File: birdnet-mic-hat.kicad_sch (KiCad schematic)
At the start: 28 parts, among them J1 PJ-327A0-SMT, J3 DF40HC(3.5)-30DS-0.4V(51), U1 TLV320ADC5140, U2 TPS7A2033PDBVR, U3 TLV3691IDCKR

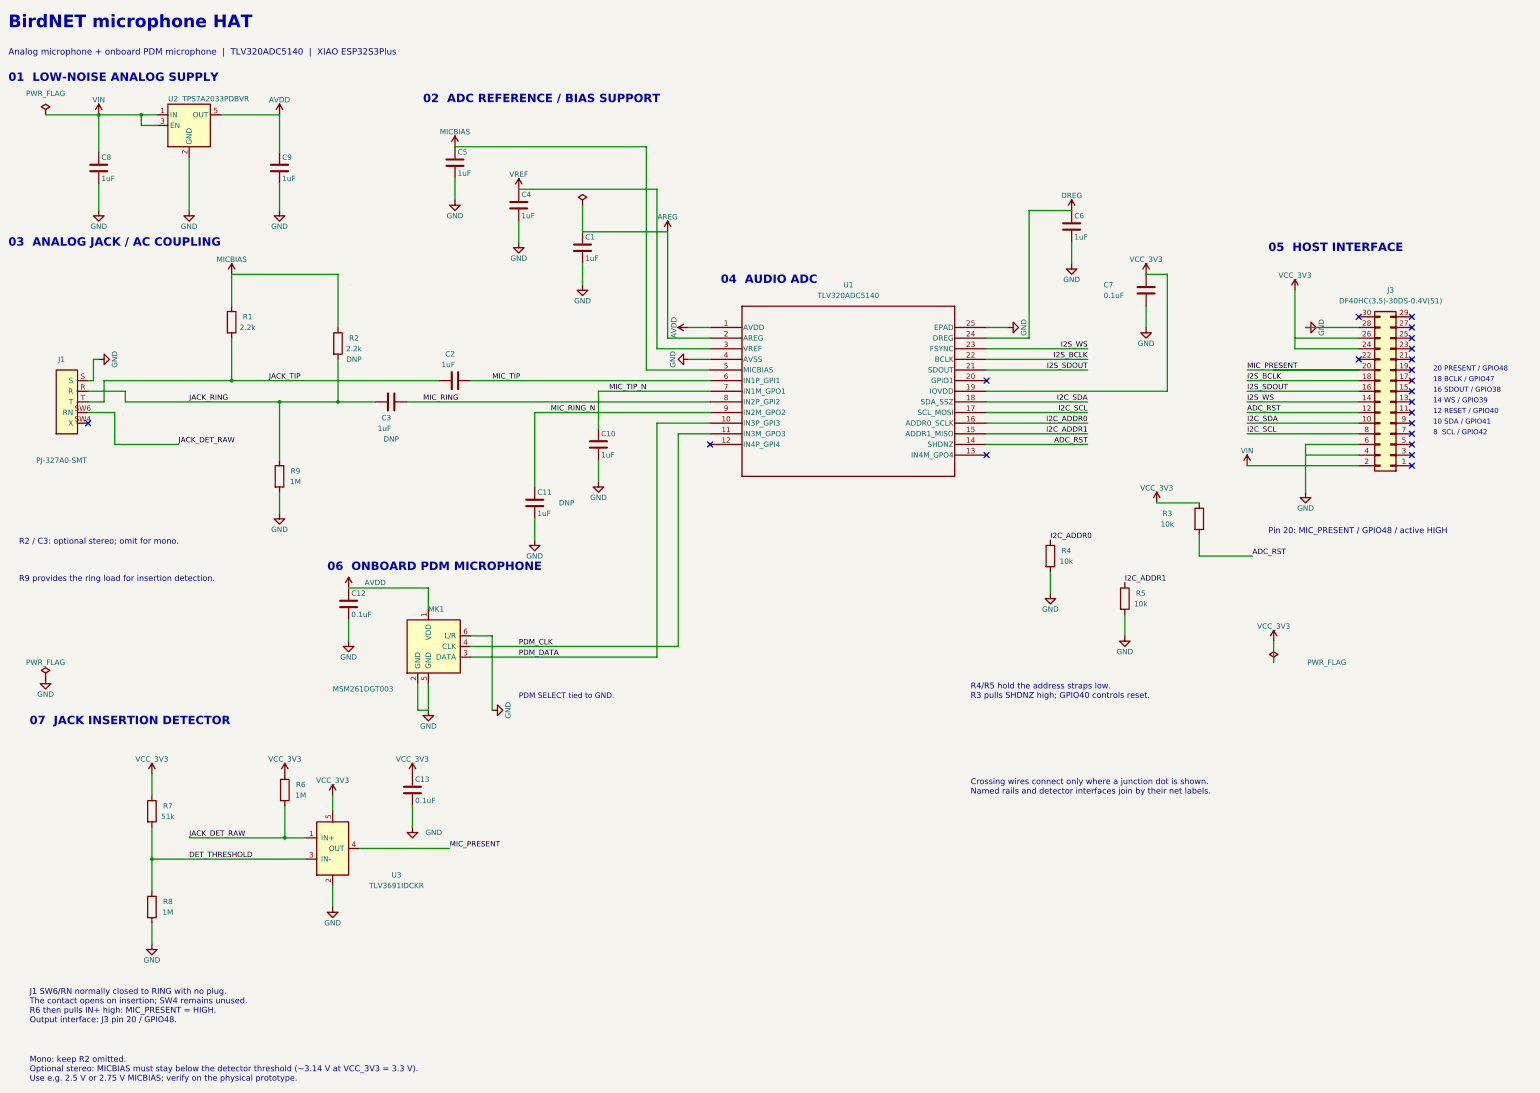
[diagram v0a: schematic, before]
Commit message: Replace jack detector comparator with transistor and removable link
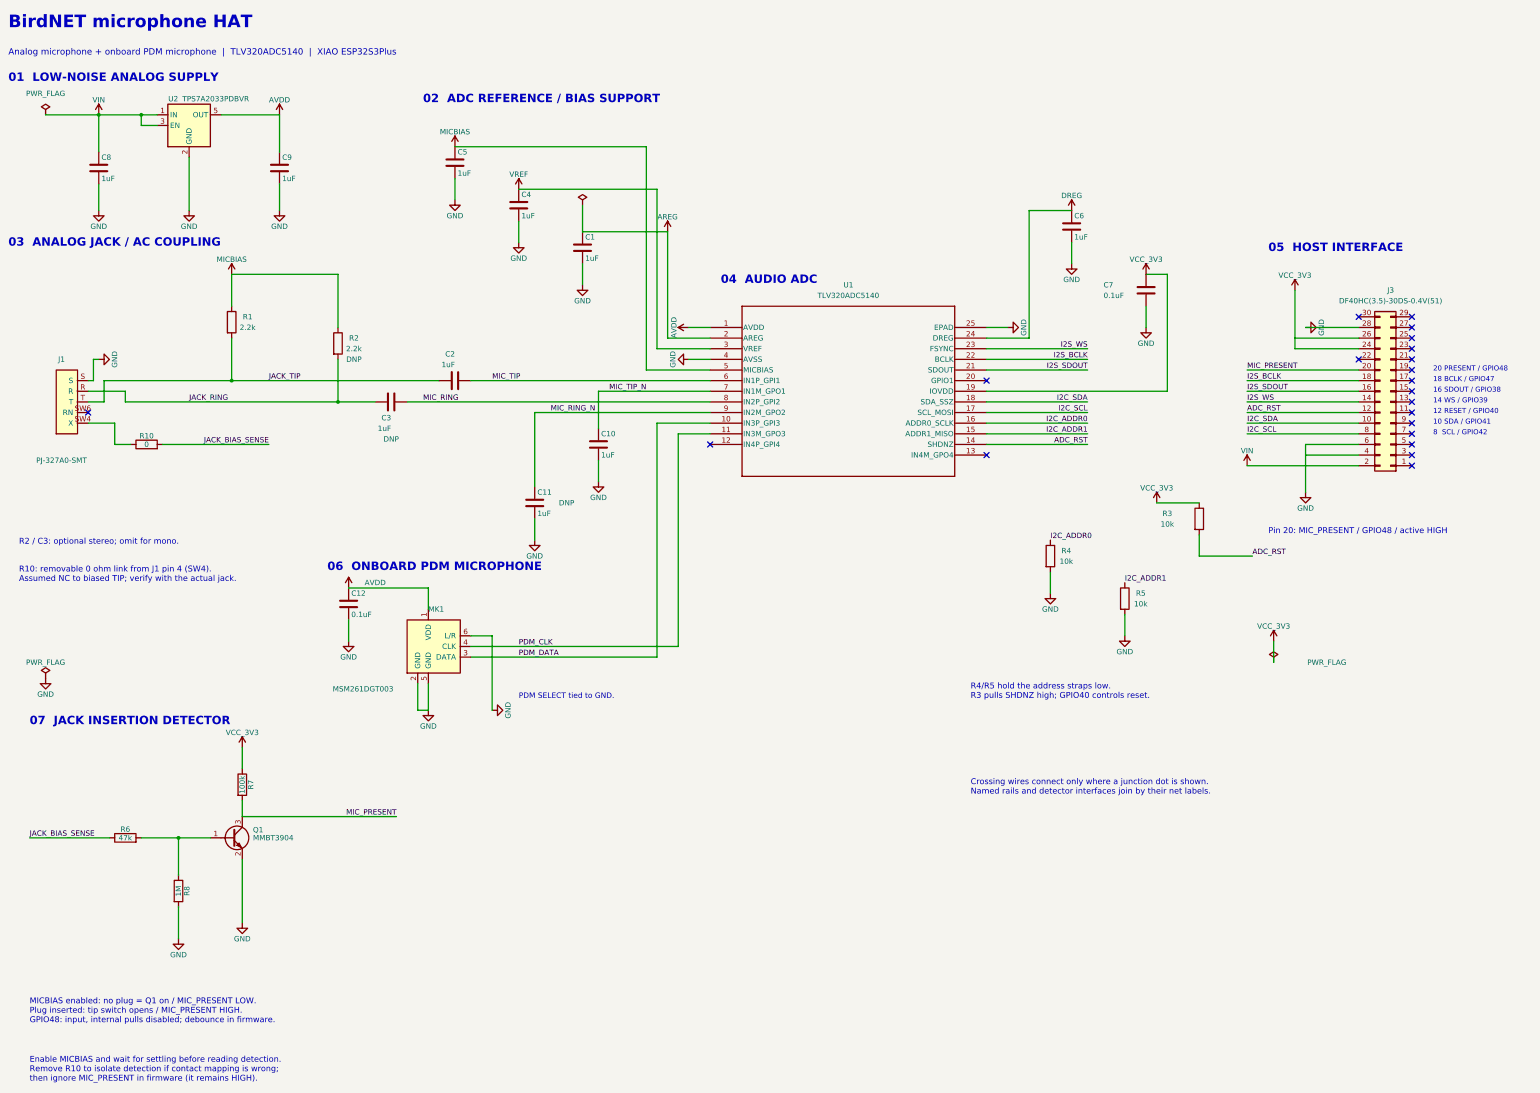
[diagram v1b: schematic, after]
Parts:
- removed C13: 0.1uF, Capacitor_SMD:C_0402_1005Metric, symbol Device:C
- removed R9: 1M, Resistor_SMD:R_0402_1005Metric, symbol Device:R
- removed U3: TLV3691IDCKR, Package_TO_SOT_SMD:SOT-353_SC-70-5, symbol BirdNetMicHat:TLV3691_SC70
- added Q1: MMBT3904, Package_TO_SOT_SMD:SOT-23, symbol Transistor_BJT:MMBT3904
- added R10: 0, Resistor_SMD:R_0603_1608Metric, symbol Device:R
- R6: value 1M -> 47k
- R7: value 51k -> 100k
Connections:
- net GND: now also Q1.2 (E)
- net MIC_PRESENT: now also R7.2, Q1.3 (C)
- net VCC_3V3: no longer R6.1
- net at J1.SW4 (X): now also R10.1
- net DET_THRESHOLD: no longer names the net of R8.1
- net DET_THRESHOLD: now also R6.2, Q1.1 (B); no longer R7.2
- net JACK_DET_RAW: no longer names the net of J1.SW6 (RN)
- net JACK_DET_RAW: no longer R6.2
- new net JACK_BIAS_SENSE: R10.2, R6.1
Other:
- note added: "Enable MICBIAS and wait for settling before reading detection. Remove R10 to isolate detection if contact mapping is wrong; then ignore MIC_PRESENT in firmware (it remains HIGH)."
- note added: "MICBIAS enabled: no plug = Q1 on / MIC_PRESENT LOW. Plug inserted: tip switch opens / MIC_PRESENT HIGH. GPIO48: input, internal pulls disabled; debounce in firmware."
- note added: "R10: removable 0 ohm link from J1 pin 4 (SW4). Assumed NC to biased TIP; verify with the actual jack."
- note removed: "J1 SW6/RN normally closed to RING with no plug. The contact opens on insertion; SW4 remains unused. R6 then pulls IN+ high: MIC_PRESENT = HIGH. Output interface: J3 pin 20 / GPIO48."
- note removed: "Mono: keep R2 omitted. Optional stereo: MICBIAS must stay below the detector threshold (~3.14 V at VCC_3V3 = 3.3 V). Use e.g. 2.5 V or 2.75 V MICBIAS; verify on the physical prototype."
- note removed: "R9 provides the ring load for insertion detection."

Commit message: Remove redundant jack detection link; retain 0402 base resistor
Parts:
- removed R10: 0, Resistor_SMD:R_0603_1608Metric, symbol Device:R
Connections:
- net JACK_BIAS_SENSE: now also J1.SW4 (X)
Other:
- note added: "Enable MICBIAS and wait for settling before reading detection. Remove R6 to isolate detection if contact mapping is wrong; then ignore MIC_PRESENT in firmware (it remains HIGH)."
- note added: "J1 pin 4 (SW4): assumed NC to biased TIP. Verify with the actual jack; remove R6 to disable detection."
- note removed: "Enable MICBIAS and wait for settling before reading detection. Remove R10 to isolate detection if contact mapping is wrong; then ignore MIC_PRESENT in firmware (it remains HIGH)."
- note removed: "R10: removable 0 ohm link from J1 pin 4 (SW4). Assumed NC to biased TIP; verify with the actual jack."
